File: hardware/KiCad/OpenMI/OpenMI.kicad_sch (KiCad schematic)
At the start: 14 parts, among them Q1 MASTERGAN1, Q2 Q_NMOS_DGS, Q3 Q_NMOS_DGS

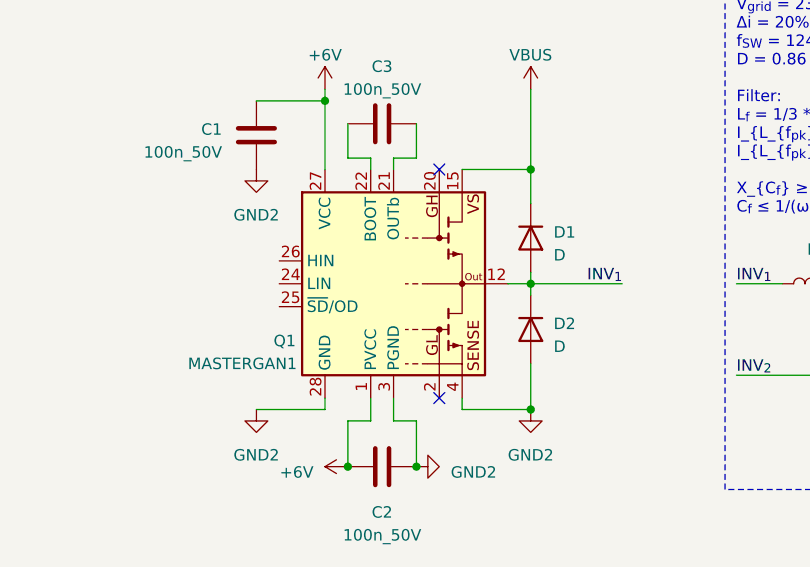
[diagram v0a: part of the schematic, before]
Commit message: hw: update symbol
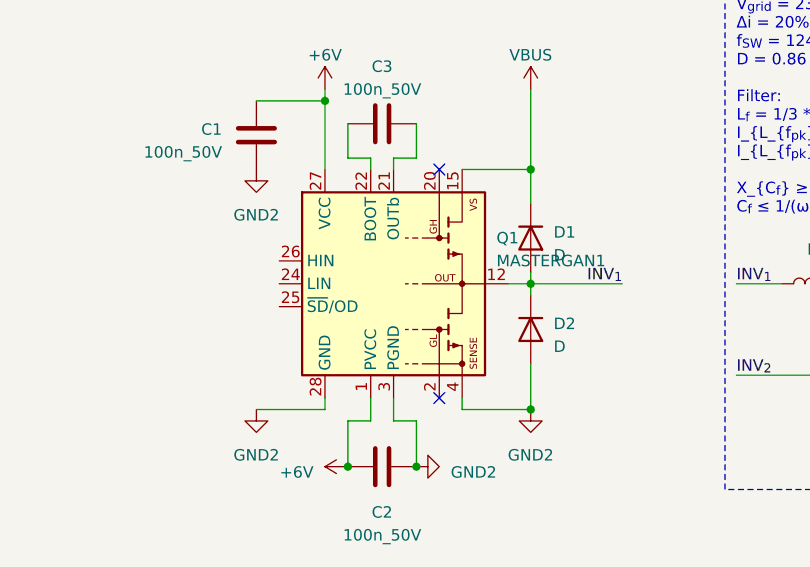
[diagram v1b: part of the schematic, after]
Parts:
- removed Q1: MASTERGAN1, symbol OpenCE:MASTERGAN1
- added Q1: MASTERGAN1, OpenCE:ST_QFN-31-3EP_9x9mm_P0.6mm, symbol _Transistor_FET:MASTERGAN1
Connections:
- net +6V: now also Q1.1 (PVCC), Q1.27 (VCC)
- net GND: now also Q1.10 (SENSE), Q1.11 (SENSE), Q1.28 (GND), Q1.3 (PGND), Q1.4, Q1.5 (SENSE), Q1.6 (SENSE), Q1.7 (SENSE), Q1.8 (SENSE), Q1.9 (SENSE), Q1.EP1 (GND), Q1.EP2 (SENSE)
- net INV_{1}: now also Q1.12, Q1.13 (OUT), Q1.14 (OUT), Q1.EP3 (OUT)
- net VBUS: now also Q1.15, Q1.16 (VS), Q1.17 (VS), Q1.18 (VS), Q1.19 (VS)
- net at C3.2: now also Q1.21 (OUTb)
- net at C3.1: now also Q1.22 (BOOT)
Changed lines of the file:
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@@
+    )
+  )
+  (symbol (lib_id "_Transistor_FET:MASTERGAN1") (at 132.08 73.66 0) (unit 1)
+    (in_bom yes) (on_board yes) (dnp no)
+    (property "Reference" "Q1" (at 143.51 68.58 0) (do_not_autoplace)
+      (effects (font (size 1.27 1.27)) (justify left))
+    )
+    (property "Value" "MASTERGAN1" (at 143.51 71.12 0) (do_not_autoplace)
+      (effects (font (size 1.27 1.27)) (justify left))
+    )
+    (property "Footprint" "OpenCE:ST_QFN-31-3EP_9x9mm_P0.6mm" (at 137.16 73.66 0)
+      (effects (font (size 1.27 1.27)) hide)
+    )
+    (property "Datasheet" "https://www.st.com/resource/en/datasheet/mastergan1.pdf" (at 137.16 73.66 0)
+      (effects (font (size 1.27 1.27)) hide)
+    )
+    (property "MF" "ST" (at 132.08 73.66 0)
+      (effects (font (size 1.27 1.27)) hide)
+    )
+    (property "MPN" "MASTERGAN1" (at 132.08 73.66 0)
+      (effects (font (size 1.27 1.27)) hide)
+    )
+    (property "OC_CONRAD" "" (at 132.08 73.66 0)
+      (effects (font (size 1.27 1.27)) hide)
+    )
+    (property "OC_FARNELL" "" (at 132.08 73.66 0)
+      (effects (font (size 1.27 1.27)) hide)
+    )
+    (property "OC_LCSC" "" (at 132.08 73.66 0)
+      (effects (font (size 1.27 1.27)) hide)
+    )
+    (property "OC_MOUSER" "511-MASTERGAN1" (at 132.08 73.66 0)
+      (effects (font (size 1.27 1.27)) hide)
+    )
+    (property "OC_REICHELT" "" (at 132.08 73.66 0)
+      (effects (font (size 1.27 1.27)) hide)
+    )
+    (pin "1")
+    (pin "10")
+    (pin "11")
+    (pin "12")
+    (pin "13")
+    (pin "14")
+    (pin "15")
+    (pin "16")
+    (pin "17")
+    (pin "18")
+    (pin "19")
+    (pin "2")
+    (pin "20")
+    (pin "21")
+    (pin "22")
+    (pin "23")
+    (pin "24")
+    (pin "25")
+    (pin "26")
+    (pin "27")
+    (pin "28")
+    (pin "29")
+    (pin "3")
+    (pin "30")
+    (pin "31")
+    (pin "4")
+    (pin "5")
+    (pin "6")
+    (pin "7")
+    (pin "8")
+    (pin "9")
+    (pin "EP1")
+    (pin "EP2")
+    (pin "EP3")
+    (instances
+      (project "OpenMI"
+        (path "/2d959e19-1572-42a0-a8fd-da8463ad4e66"
+          (reference "Q1") (unit 1)
+        )
+      )
     )
   )
@@
         )
       )
-    )
-  )
-  (symbol (lib_id "OpenCE:MASTERGAN1") (at 132.08 73.66 0) (unit 1)
-    (in_bom yes) (on_board yes) (dnp no)
-    (property "Reference" "Q1" (at 118.745 80.01 0) (do_not_autoplace)
-      (effects (font (size 1.27 1.27)) (justify left))
-    )
-    (property "Value" "MASTERGAN1" (at 109.22 82.55 0) (do_not_autoplace)
-      (effects (font (size 1.27 1.27)) (justify left))
-    )
-    (property "Footprint" "" (at 137.16 73.66 0)
-      (effects (font (size 1.27 1.27)) hide)
-    )
-    (property "Datasheet" "https://www.st.com/resource/en/datasheet/mastergan1.pdf" (at 137.16 73.66 0)
-      (effects (font (size 1.27 1.27)) hide)
-    )
-    (pin "1")
-    (pin "10")
-    (pin "11")
-    (pin "12")
-    (pin "13")
-    (pin "14")
-    (pin "15")
-    (pin "16")
-    (pin "17")
-    (pin "18")
-    (pin "19")
-    (pin "2")
-    (pin "20")
-    (pin "21")
-    (pin "22")
-    (pin "23")
-    (pin "24")
-    (pin "25")
-    (pin "26")
-    (pin "27")
-    (pin "28")
-    (pin "29")
-    (pin "3")
-    (pin "30")
-    (pin "31")
-    (pin "4")
-    (pin "5")
-    (pin "6")
-    (pin "7")
-    (pin "8")
-    (pin "9")
-    (pin "EP1")
-    (pin "EP2")
-    (pin "EP3")
-    (instances
-      (project "OpenMI"
-        (path "/2d959e19-1572-42a0-a8fd-da8463ad4e66"
-          (reference "Q1") (unit 1)
-        )
-      )

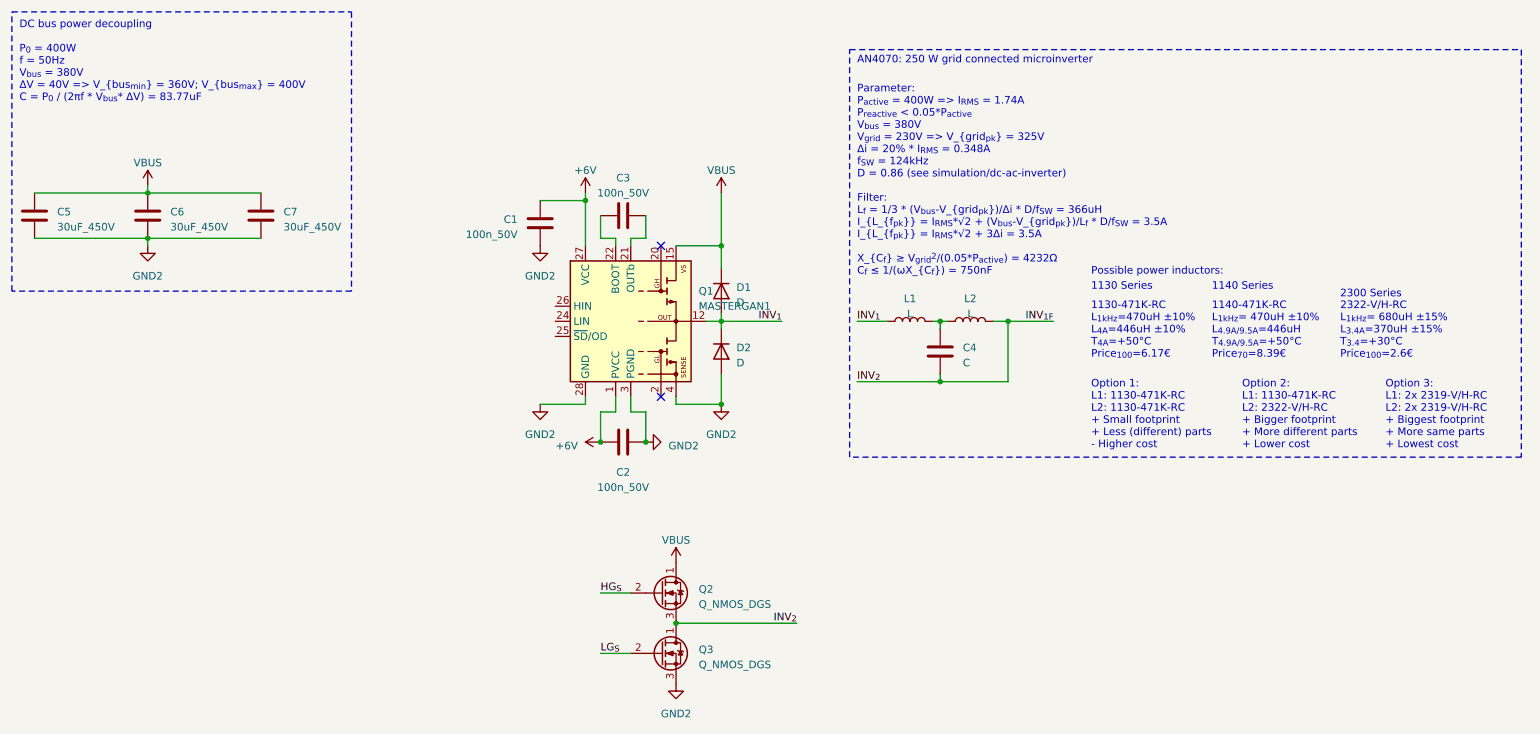
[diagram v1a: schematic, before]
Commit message: hw: add sheets to separate concerns
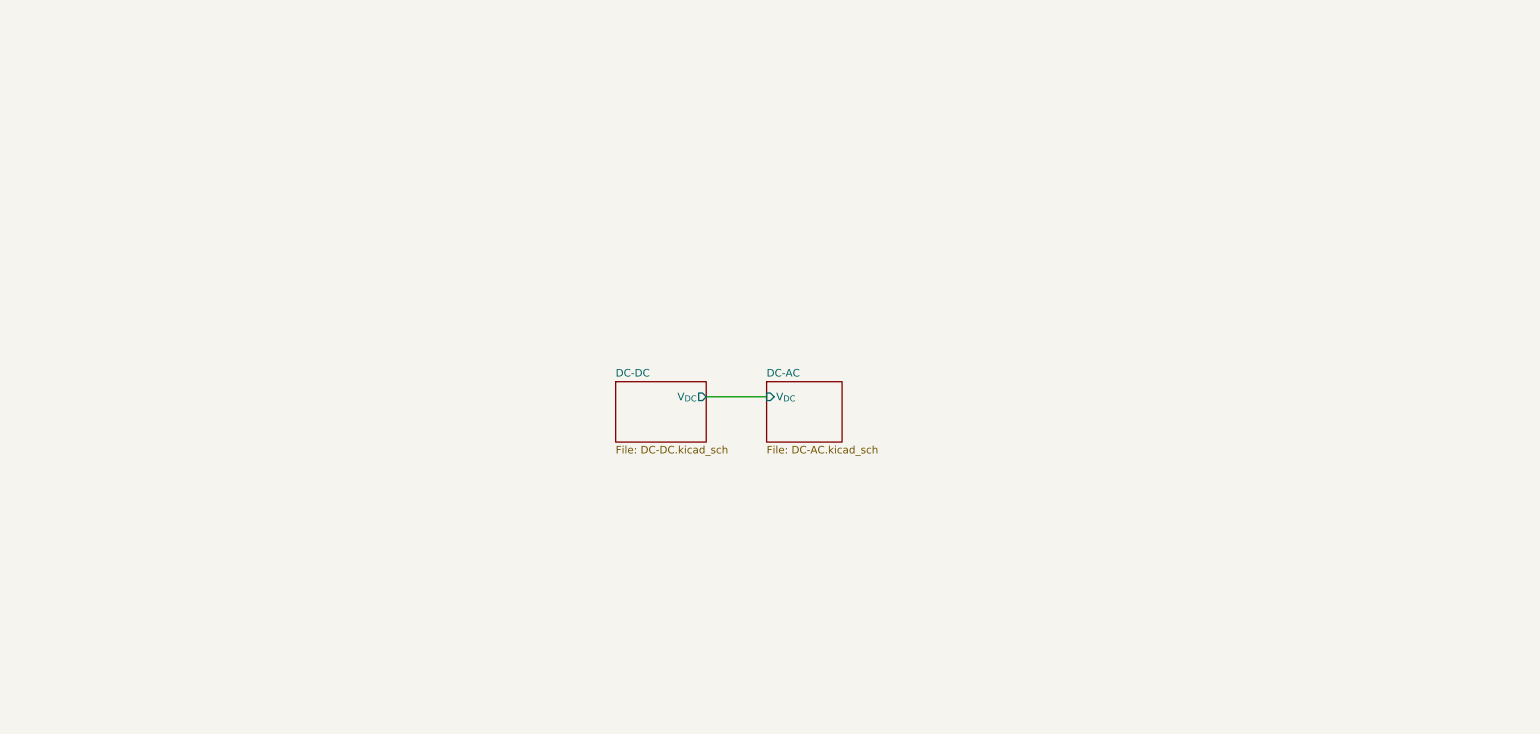
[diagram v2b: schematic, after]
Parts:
- removed C1, C2, C3: 100n_50V, Capacitor_SMD:C_0603_1608Metric, symbol _C_0603:100n_50V
- removed C4: C, symbol Device:C
- removed C5, C6, C7: 30uF_450V, OpenCE:C_Rect_L43mm_W42mm_H25mm_P37.5mm_P20.3mm_KEMET, symbol _C_Film:30uF_450V
- removed D1, D2: D, symbol Device:D
- removed L1, L2: L, symbol Device:L
- removed Q1: MASTERGAN1, OpenCE:ST_QFN-31-3EP_9x9mm_P0.6mm, symbol _Transistor_FET:MASTERGAN1
- removed Q2, Q3: Q_NMOS_DGS, symbol Device:Q_NMOS_DGS
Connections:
- no-connect marks 2 -> 0
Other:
- added sheet DC-AC (DC-AC.kicad_sch)
- added sheet DC-DC (DC-DC.kicad_sch)
- note removed: "1130 Series"
- note removed: "1130-471K-RC L_{1kHz}=470uH ±10% L_{4A}=446uH ±10% T_{4A}=+50°C Price_{100}=6.17€"
- note removed: "1140 Series"
- note removed: "1140-471K-RC L_{1kHz}= 470uH ±10% L_{4.9A/9.5A}=446uH T_{4.9A/9.5A}=+50°C Price_{70}=8.39€"
- note removed: "2300 Series"
- note removed: "2322-V/H-RC L_{1kHz}= 680uH ±15% L_{3.4A}=370uH ±15% T_{3.4}=+30°C Price_{100}=2.6€"
- note removed: "AN4070: 250 W grid connected microinverter"
- note removed: "DC bus power decoupling P_{0} = 400W f = 50Hz V_{bus} = 380V ΔV = 40V => V_{bus_{min}} = 360V; V_{bus_{max}} = 400V C = P_{0} / (2πf * V_{bus}* ΔV) = 83.77uF"
- note removed: "Option 1: L1: 1130-471K-RC L2: 1130-471K-RC + Small footprint + Less (different) parts - Higher cost"
- note removed: "Option 2: L1: 1130-471K-RC L2: 2322-V/H-RC + Bigger footprint + More different parts + Lower cost"
- note removed: "Option 3: L1: 2x 2319-V/H-RC L2: 2x 2319-V/H-RC + Biggest footprint + More same parts + Lowest cost"
- note removed: "Parameter: P_{active} = 400W => I_{RMS} = 1.74A P_{reactive} < 0.05*P_{active} V_{bus} = 380V V_{grid} = 230V => V_{grid_{pk}} = 325V Δi = 20% * I_{RMS} = 0.348A f_{SW} = 124kHz D = 0.86 (see simulation/dc-ac-inverter) Filter: L_{f} = 1/3 * (V_{bus}-V_{grid_{pk}})/Δi * D/f_{SW} = 366uH I_{L_{f_{pk}}} = I_{RMS}*√2 + (V_{bus}-V_{grid_{pk}})/L_{f} * D/f_{SW} = 3.5A I_{L_{f_{pk}}} = I_{RMS}*√2 + 3Δi 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"
- note removed: "Possible power inductors:"

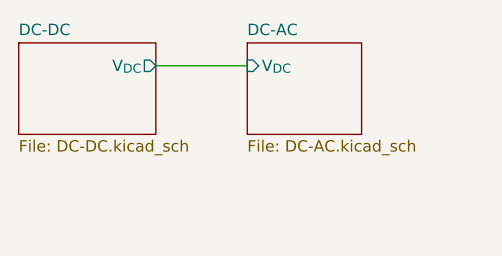
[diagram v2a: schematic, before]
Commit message: feat(hw): Add slow leg of DC-AC inverter
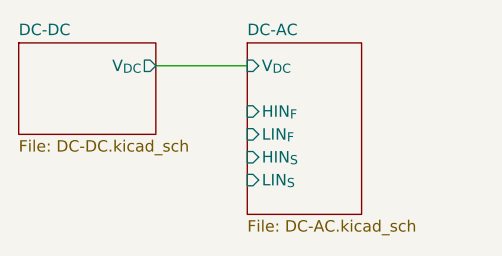
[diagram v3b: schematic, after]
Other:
- sheet DC-AC ports: added HIN_{F}, HIN_{S}, LIN_{F}, LIN_{S}; removed none
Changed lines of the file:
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@@
     (stroke (width 0) (type default))
   )
-  (sheet (at 154.94 83.82) (size 12.7 10.16) (fields_autoplaced)
+  (sheet (at 154.94 83.82) (size 12.7 19.05) (fields_autoplaced)
     (stroke (width 0.1524) (type solid))
     (fill (color 0 0 0 0.0000))
@@
       (effects (font (size 1.27 1.27)) (justify left bottom))
     )
-    (property "Sheetfile" "DC-AC.kicad_sch" (at 154.94 94.5646 0)
+    (property "Sheetfile" "DC-AC.kicad_sch" (at 154.94 103.4546 0)
       (effects (font (size 1.27 1.27)) (justify left top))
     )
@@
       (effects (font (size 1.27 1.27)) (justify left))
     )
+    (pin "LIN_{S}" input (at 154.94 99.06 180)
+      (effects (font (size 1.27 1.27)) (justify left))
+    )
+    (pin "HIN_{S}" input (at 154.94 96.52 180)
+      (effects (font (size 1.27 1.27)) (justify left))
+    )
+    (pin "HIN_{F}" input (at 154.94 91.44 180)
+      (effects (font (size 1.27 1.27)) (justify left))
+    )
+    (pin "LIN_{F}" input (at 154.94 93.98 180)
+      (effects (font (size 1.27 1.27)) (justify left))
+    )

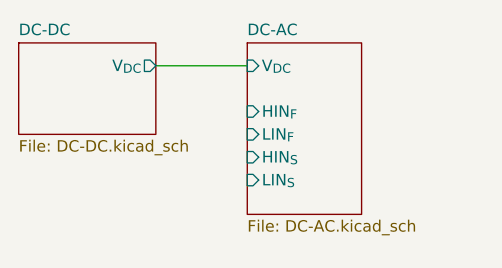
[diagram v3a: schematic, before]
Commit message: feat(hw): Add over temperature output
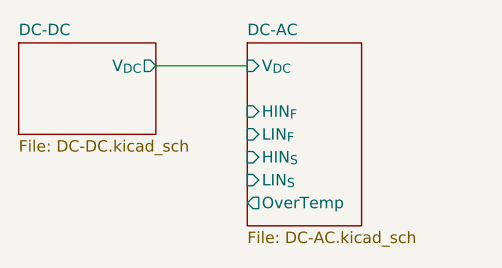
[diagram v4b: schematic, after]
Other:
- sheet DC-AC ports: added OverTemp; removed none
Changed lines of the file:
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@@
     (stroke (width 0) (type default))
   )
-  (sheet (at 154.94 83.82) (size 12.7 19.05) (fields_autoplaced)
+  (sheet (at 154.94 83.82) (size 12.7 20.32) (fields_autoplaced)
     (stroke (width 0.1524) (type solid))
     (fill (color 0 0 0 0.0000))
@@
       (effects (font (size 1.27 1.27)) (justify left bottom))
     )
-    (property "Sheetfile" "DC-AC.kicad_sch" (at 154.94 103.4546 0)
+    (property "Sheetfile" "DC-AC.kicad_sch" (at 154.94 104.7246 0)
       (effects (font (size 1.27 1.27)) (justify left top))
     )
@@
       (effects (font (size 1.27 1.27)) (justify left))
     )
+    (pin "OverTemp" output (at 154.94 101.6 180)
+      (effects (font (size 1.27 1.27)) (justify left))
+    )

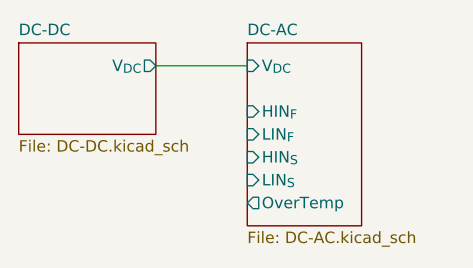
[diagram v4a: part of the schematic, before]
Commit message: feat(hw): Add input capacitance and inductor suggestions
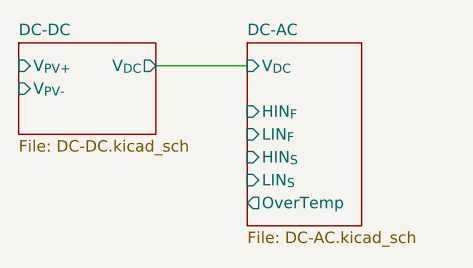
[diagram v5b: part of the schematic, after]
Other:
- sheet DC-DC ports: added V_{PV+}, V_{PV-}; removed none
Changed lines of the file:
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@@
       (effects (font (size 1.27 1.27)) (justify right))
+    )
+    (pin "V_{PV+}" input (at 129.54 86.36 180)
+      (effects (font (size 1.27 1.27)) (justify left))
+    )
+    (pin "V_{PV-}" input (at 129.54 88.9 180)
+      (effects (font (size 1.27 1.27)) (justify left))
     )
     (instances

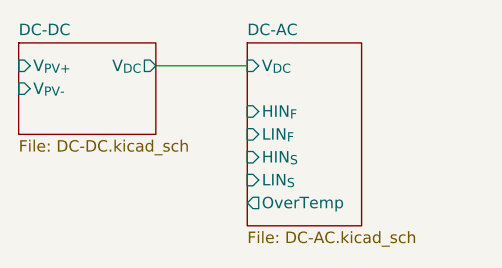
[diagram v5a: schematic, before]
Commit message: refactor(hw): Rename hierarchical label V_DC -> V_BUS
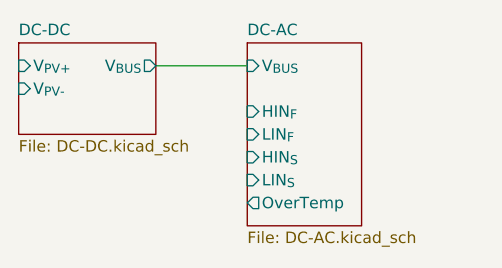
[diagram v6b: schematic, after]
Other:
- sheet DC-AC ports: added V_{BUS}; removed V_{DC}
- sheet DC-DC ports: added V_{BUS}; removed V_{DC}
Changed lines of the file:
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@@
       (effects (font (size 1.27 1.27)) hide)
-    )
-    (pin "V_{DC}" input (at 154.94 86.36 180)
-      (effects (font (size 1.27 1.27)) (justify left))
     )
     (pin "LIN_{S}" input (at 154.94 99.06 180)
@@
     )
     (pin "OverTemp" output (at 154.94 101.6 180)
+      (effects (font (size 1.27 1.27)) (justify left))
+    )
+    (pin "V_{BUS}" input (at 154.94 86.36 180)
       (effects (font (size 1.27 1.27)) (justify left))
     )
@@
       (effects (font (size 1.27 1.27)) hide)
     )
-    (pin "V_{DC}" output (at 144.78 86.36 0)
-      (effects (font (size 1.27 1.27)) (justify right))
-    )
     (pin "V_{PV+}" input (at 129.54 86.36 180)
       (effects (font (size 1.27 1.27)) (justify left))
@@
       (effects (font (size 1.27 1.27)) (justify left))
     )
+    (pin "V_{BUS}" output (at 144.78 86.36 0)
+      (effects (font (size 1.27 1.27)) (justify right))
+    )
     (instances

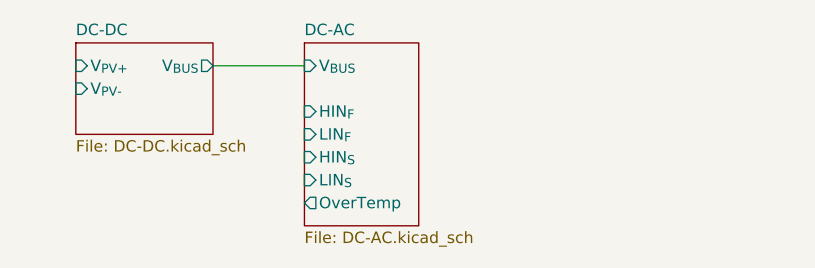
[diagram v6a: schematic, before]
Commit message: feat(hw): Adds new "Grid" sheet. Adds grid voltage sense
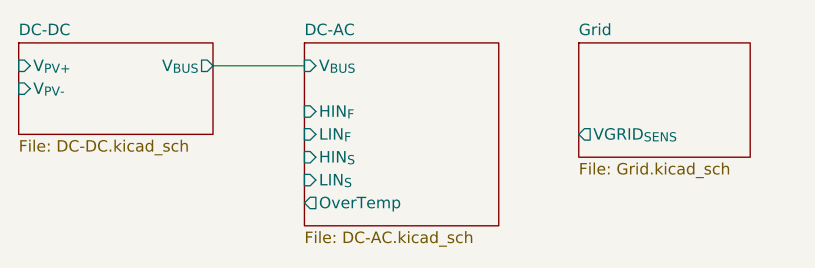
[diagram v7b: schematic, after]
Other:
- added sheet Grid (Grid.kicad_sch)
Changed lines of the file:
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@@
     (stroke (width 0) (type default))
   )
-  (sheet (at 154.94 83.82) (size 12.7 20.32) (fields_autoplaced)
+  (sheet (at 154.94 83.82) (size 21.59 20.32) (fields_autoplaced)
     (stroke (width 0.1524) (type solid))
     (fill (color 0 0 0 0.0000))
@@
     )
   )
-  (sheet (at 129.54 83.82) (size 15.24 10.16) (fields_autoplaced)
+  (sheet (at 185.42 83.82) (size 19.05 12.7) (fields_autoplaced)
     (stroke (width 0.1524) (type solid))
     (fill (color 0 0 0 0.0000))
-    (property "Sheetname" "DC-DC" (at 129.54 83.1084 0)
+    (property "Sheetname" "Grid" (at 185.42 83.1084 0)
       (effects (font (size 1.27 1.27)) (justify left bottom))
     )
-    (property "Sheetfile" "DC-DC.kicad_sch" (at 129.54 94.5646 0)
+    (property "Sheetfile" "Grid.kicad_sch" (at 185.42 97.1046 0)
       (effects (font (size 1.27 1.27)) (justify left top))
     )
-    (property "Field2" "" (at 129.54 83.82 0)
+    (property "Field2" "" (at 185.42 83.82 0)
       (effects (font (size 1.27 1.27)) hide)
     )
-    (pin "V_{PV+}" input (at 129.54 86.36 180)
+    (pin "VGRID_{SENS}" output (at 185.42 93.98 180)
       (effects (font (size 1.27 1.27)) (justify left))
     )
-    (pin "V_{PV-}" input (at 129.54 88.9 180)
+    (instances
+      (project "OpenMI"
+        (path "/2d959e19-1572-42a0-a8fd-da8463ad4e66" (page "4"))
+      )
+    )
+  )
+  (sheet (at 123.19 83.82) (size 21.59 10.16) (fields_autoplaced)
+    (stroke (width 0.1524) (type solid))
+    (fill (color 0 0 0 0.0000))
+    (property "Sheetname" "DC-DC" (at 123.19 83.1084 0)
+      (effects (font (size 1.27 1.27)) (justify left bottom))
+    )
+    (property "Sheetfile" "DC-DC.kicad_sch" (at 123.19 94.5646 0)
+      (effects (font (size 1.27 1.27)) (justify left top))
+    )
+    (property "Field2" "" (at 123.19 83.82 0)
+      (effects (font (size 1.27 1.27)) hide)
+    )
+    (pin "V_{PV+}" input (at 123.19 86.36 180)
       (effects (font (size 1.27 1.27)) (justify left))
     )
+    (pin "V_{PV-}" input (at 123.19 88.9 180)
+      (effects (font (size 1.27 1.27)) (justify left))
+    )
